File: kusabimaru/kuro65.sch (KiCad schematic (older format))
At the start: 20 parts, among them IC1 ATMEGA32U4, J1 ISP, J2 USB4085-GF-A, SW1 SW_Push, Y1 16MHz

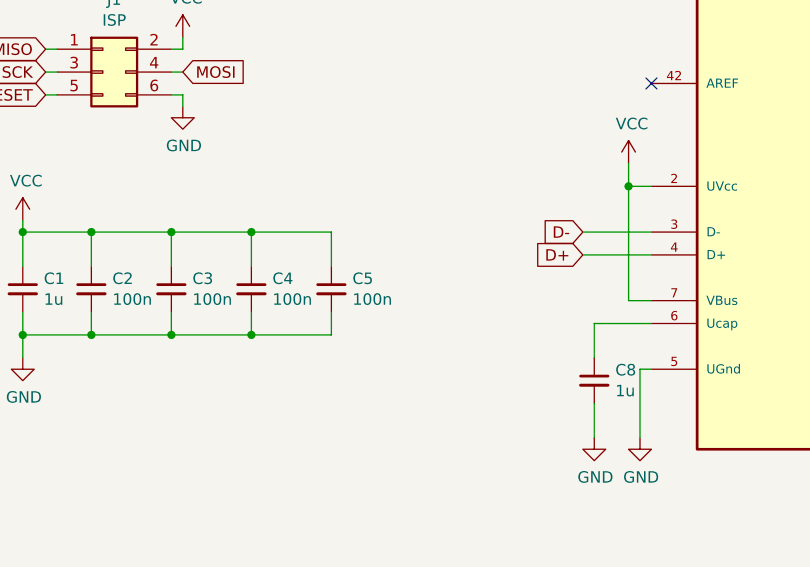
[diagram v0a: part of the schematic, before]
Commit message: Initial component placement done
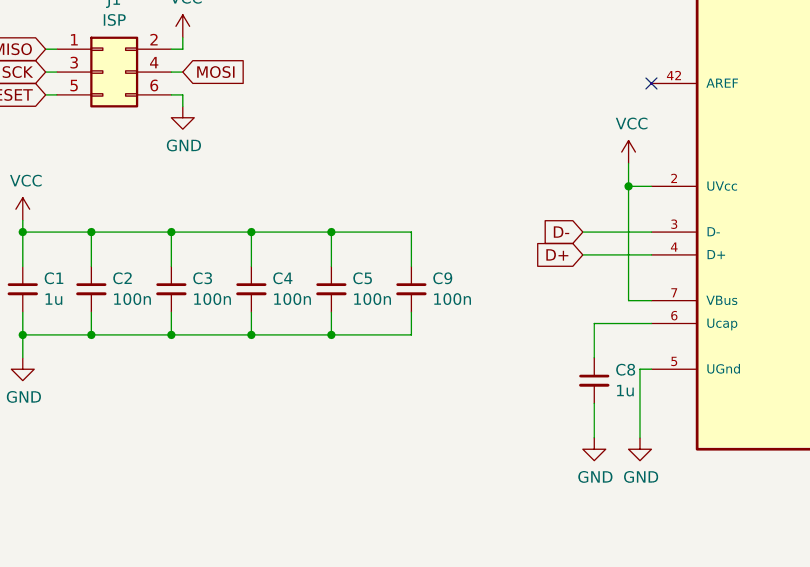
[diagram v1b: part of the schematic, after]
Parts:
- added C9: 100n, Capacitor_SMD:C_0805_2012Metric_Pad1.18x1.45mm_HandSolder, symbol Device:C_Small
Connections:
- net GND: now also C9.2
- net VCC: now also C9.1
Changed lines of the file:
@@
 Wire Wire Line
 	1950 1050 1950 1000
+$Comp
+L Device:C_Small C9
+U 1 1 602AC3E9
+P 2550 4300
+F 0 "C9" H 2642 4346 50  0000 L CNN
+F 1 "100n" H 2642 4255 50  0000 L CNN
+F 2 "Capacitor_SMD:C_0805_2012Metric_Pad1.18x1.45mm_HandSolder" H 2550 4300 50  0001 C CNN
+F 3 "~" H 2550 4300 50  0001 C CNN
+	1    2550 4300
+	1    0    0    -1
+$EndComp
+Wire Wire Line
+	2200 4050 2550 4050
+Wire Wire Line
+	2550 4050 2550 4200
+Connection ~ 2200 4050
+Wire Wire Line
+	2200 4500 2550 4500
+Wire Wire Line
+	2550 4500 2550 4400
+Connection ~ 2200 4500
 $EndSCHEMATC

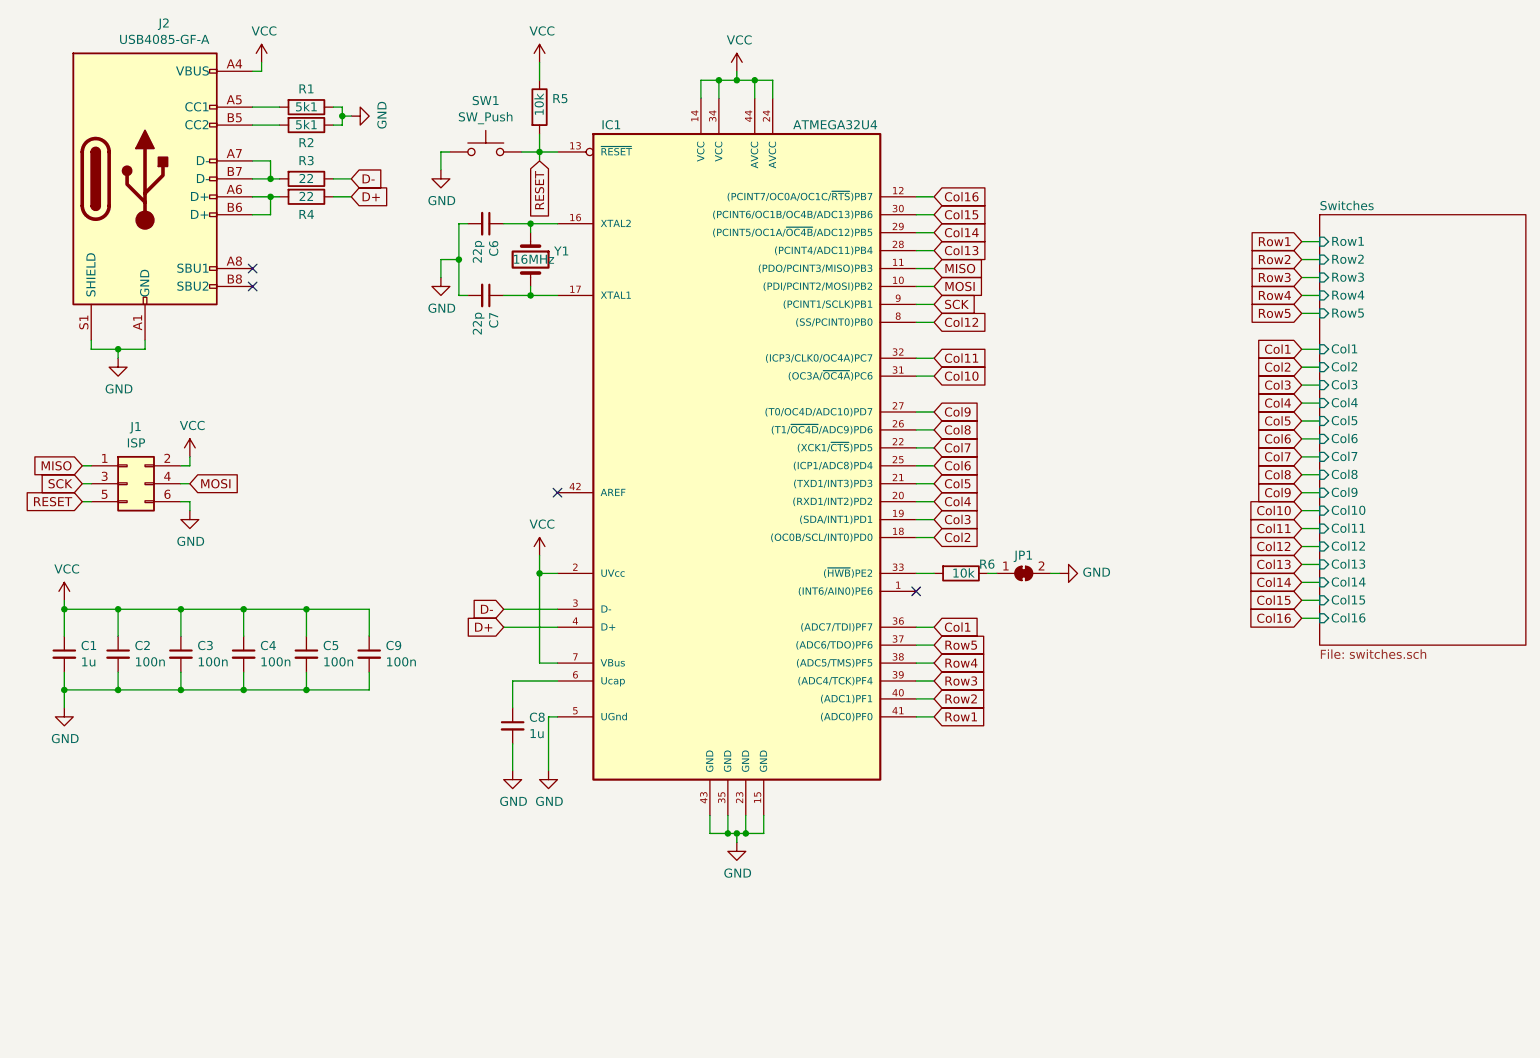
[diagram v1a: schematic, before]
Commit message: Some routing done + References added
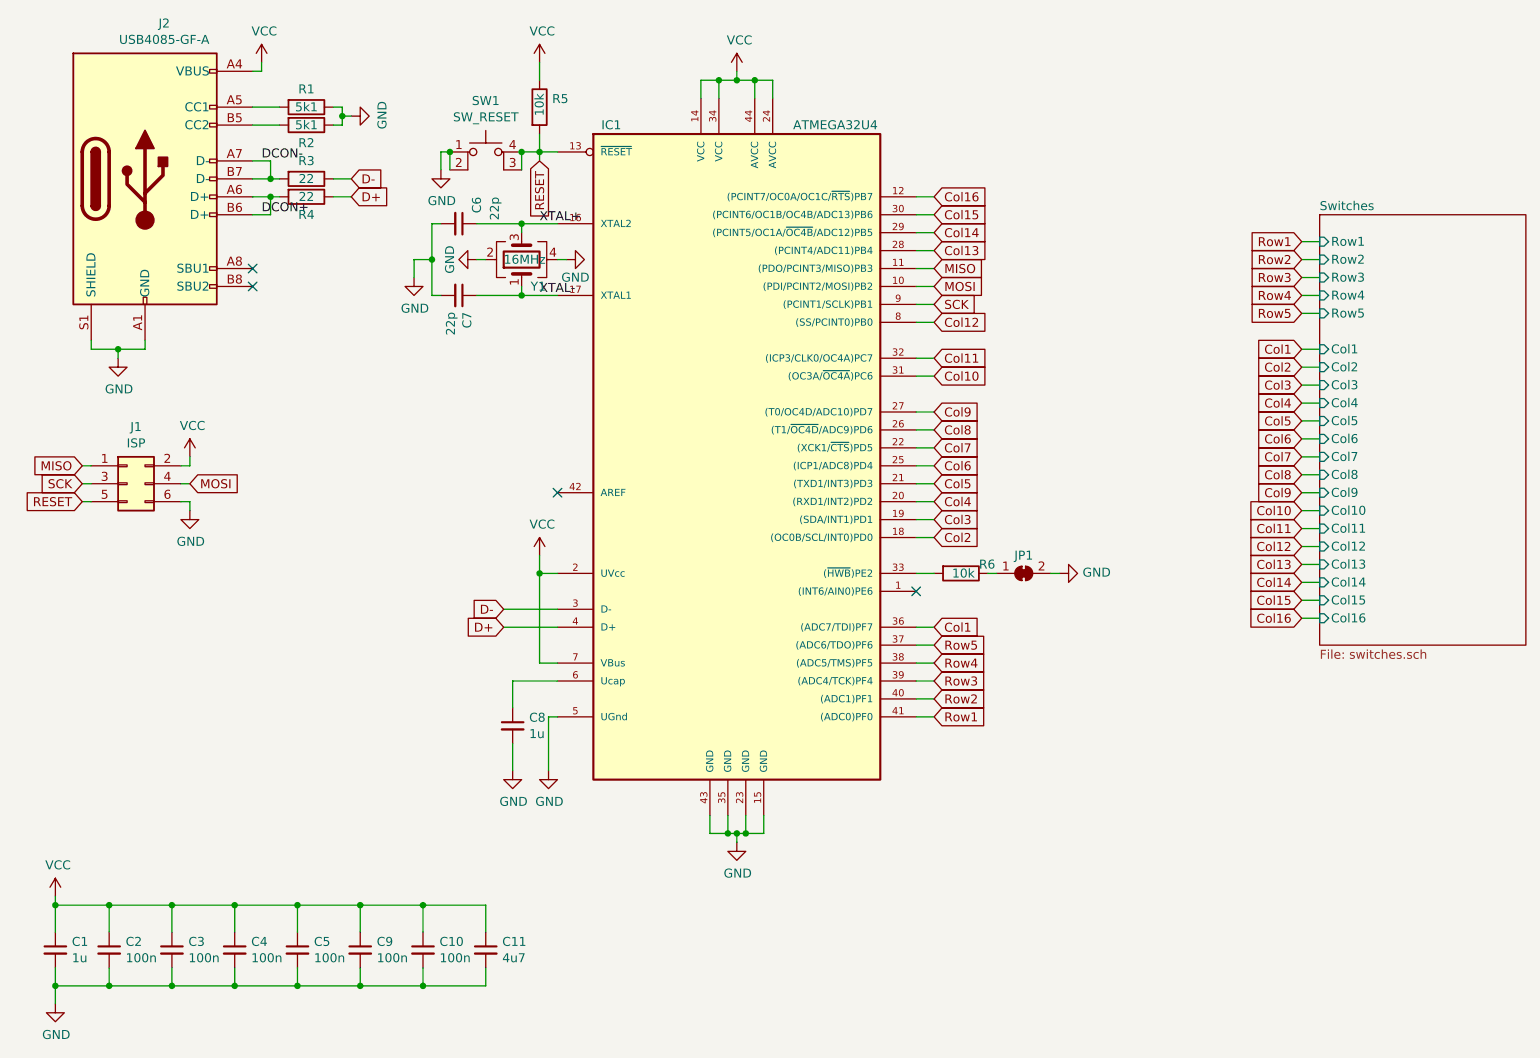
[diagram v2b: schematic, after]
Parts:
- removed SW1: SW_Push, Button_Switch_SMD:SW_SPST_Omron_B3FS-100xP, symbol Switch:SW_Push
- removed Y1: 16MHz, Crystal:Crystal_SMD_3225-4Pin_3.2x2.5mm_HandSoldering, symbol Device:Crystal
- added C10: 100n, Capacitor_SMD:C_0805_2012Metric_Pad1.18x1.45mm_HandSolder, symbol Device:C_Small
- added C11: 4u7, Capacitor_SMD:C_0805_2012Metric_Pad1.18x1.45mm_HandSolder, symbol Device:C_Small
- added SW1: SW_RESET, Button_Switch_SMD:SW_SPST_Omron_B3FS-100xP, symbol Switch:SW_MEC_5E
- added Y1: 16MHz, Crystal:Crystal_SMD_SeikoEpson_TSX3225-4Pin_3.2x2.5mm_HandSoldering, symbol Device:Crystal_GND24
- C8: footprint Diode_SMD:D_0805_2012Metric_Pad1.15x1.40mm_HandSolder -> Capacitor_SMD:C_0805_2012Metric_Pad1.18x1.45mm_HandSolder
- J1: footprint Connector_PinHeader_1.27mm:PinHeader_2x03_P1.27mm_Vertical -> Connector_PinHeader_2.54mm:PinHeader_2x03_P2.54mm_Vertical
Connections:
- net GND: now also C10.2, C11.2, SW1.1, SW1.2, Y1.2, Y1.4
- net RESET: now also SW1.3 (K), SW1.4 (A)
- net VCC: now also C10.1, C11.1
- net XTAL+: now reaches C6.1, IC1.16 (XTAL2)
- net XTAL+: now also Y1.3
- net XTAL-: now reaches C7.1, IC1.17 (XTAL1)
- net XTAL-: now also Y1.1
- net DCON-: now reaches J2.A7 (D-), J2.B7 (D-), R3.2
- net DCON+: now reaches J2.A6 (D+), J2.B6 (D+), R4.2
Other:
- moved on the sheet: C1, C2, C3, C4, C5, C6, C7, C9

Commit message: Routing completed. Some modifications still needed.
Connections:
- net Col1: now also IC1.8 ((SS/PCINT0)PB0); no longer IC1.36 ((ADC7/TDI)PF7)
- net Col10: now also IC1.27 ((T0/OC4D/ADC10)PD7); no longer IC1.31 ((OC3A/~OC4A~)PC6)
- net Col11: now also IC1.28 ((PCINT4/ADC11)PB4); no longer IC1.32 ((ICP3/CLK0/OC4A)PC7)
- net Col12: now also IC1.29 ((PCINT5/OC1A/~OC4B~/ADC12)PB5); no longer IC1.8 ((SS/PCINT0)PB0)
- net Col13: now also IC1.30 ((PCINT6/OC1B/OC4B/ADC13)PB6); no longer IC1.28 ((PCINT4/ADC11)PB4)
- net Col14: now also IC1.31 ((OC3A/~OC4A~)PC6); no longer IC1.29 ((PCINT5/OC1A/~OC4B~/ADC12)PB5)
- net Col15: now also IC1.32 ((ICP3/CLK0/OC4A)PC7); no longer IC1.30 ((PCINT6/OC1B/OC4B/ADC13)PB6)
- net Col16: now also IC1.36 ((ADC7/TDI)PF7); no longer IC1.12 ((PCINT7/OC0A/OC1C/~RTS~)PB7)
- net Col2: now also IC1.12 ((PCINT7/OC0A/OC1C/~RTS~)PB7); no longer IC1.18 ((OC0B/SCL/INT0)PD0)
- net Col3: now also IC1.18 ((OC0B/SCL/INT0)PD0); no longer IC1.19 ((SDA/INT1)PD1)
- net Col4: now also IC1.19 ((SDA/INT1)PD1); no longer IC1.20 ((RXD1/INT2)PD2)
- net Col5: now also IC1.20 ((RXD1/INT2)PD2); no longer IC1.21 ((TXD1/INT3)PD3)
- net Col6: now also IC1.21 ((TXD1/INT3)PD3); no longer IC1.25 ((ICP1/ADC8)PD4)
- net Col8: now also IC1.25 ((ICP1/ADC8)PD4); no longer IC1.26 ((T1/~OC4D~/ADC9)PD6)
- net Col9: now also IC1.26 ((T1/~OC4D~/ADC9)PD6); no longer IC1.27 ((T0/OC4D/ADC10)PD7)
- net Row1: now also IC1.37 ((ADC6/TDO)PF6); no longer IC1.41 ((ADC0)PF0)
- net Row2: now also IC1.38 ((ADC5/TMS)PF5); no longer IC1.40 ((ADC1)PF1)
- net Row4: now also IC1.40 ((ADC1)PF1); no longer IC1.38 ((ADC5/TMS)PF5)
- net Row5: now also IC1.41 ((ADC0)PF0); no longer IC1.37 ((ADC6/TDO)PF6)
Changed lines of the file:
@@
 F22 "Col16" I L 7850 4100 50
 $EndSheet
-Text GLabel 5700 4650 2    50   Input ~ 0
+Text GLabel 5700 4250 2    50   Input ~ 0
 Row1
-Text GLabel 5700 4550 2    50   Input ~ 0
+Text GLabel 5700 4350 2    50   Input ~ 0
 Row2
 Text GLabel 5700 4450 2    50   Input ~ 0
 Row3
-Text GLabel 5700 4350 2    50   Input ~ 0
+Text GLabel 5700 4550 2    50   Input ~ 0
 Row4
-Text GLabel 5700 4250 2    50   Input ~ 0
+Text GLabel 5700 4650 2    50   Input ~ 0
 Row5
 Wire Wire Line
@@
 Wire Wire Line
 	7850 2000 7750 2000
-Text GLabel 5700 4150 2    50   Input ~ 0
+Text GLabel 5700 2450 2    50   Input ~ 0
 Col1
+Text GLabel 5700 1750 2    50   Input ~ 0
+Col2
 Text GLabel 5700 3650 2    50   Input ~ 0
-Col2
+Col3
 Text GLabel 5700 3550 2    50   Input ~ 0
-Col3
+Col4
 Text GLabel 5700 3450 2    50   Input ~ 0
-Col4
+Col5
 Text GLabel 5700 3350 2    50   Input ~ 0
-Col5
-Text GLabel 5700 3250 2    50   Input ~ 0
 Col6
 Text GLabel 5700 3150 2    50   Input ~ 0
 Col7
+Text GLabel 5700 3250 2    50   Input ~ 0
+Col8
 Text GLabel 5700 3050 2    50   Input ~ 0
-Col8
+Col9
 Text GLabel 5700 2950 2    50   Input ~ 0
-Col9
+Col10
+Text GLabel 5700 2050 2    50   Input ~ 0
+Col11
+Text GLabel 5700 1950 2    50   Input ~ 0
+Col12
+Text GLabel 5700 1850 2    50   Input ~ 0
+Col13
 Text GLabel 5700 2750 2    50   Input ~ 0
-Col10
+Col14
 Text GLabel 5700 2650 2    50   Input ~ 0
-Col11
-Text GLabel 5700 2450 2    50   Input ~ 0
-Col12
-Text GLabel 5700 2050 2    50   Input ~ 0
-Col13
-Text GLabel 5700 1950 2    50   Input ~ 0
-Col14
-Text GLabel 5700 1850 2    50   Input ~ 0
 Col15
-Text GLabel 5700 1750 2    50   Input ~ 0
+Text GLabel 5700 4150 2    50   Input ~ 0
 Col16
 Wire Wire Line
